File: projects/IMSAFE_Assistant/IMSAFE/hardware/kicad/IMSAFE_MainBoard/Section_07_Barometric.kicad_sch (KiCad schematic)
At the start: 3 parts, among them U9 BMP390

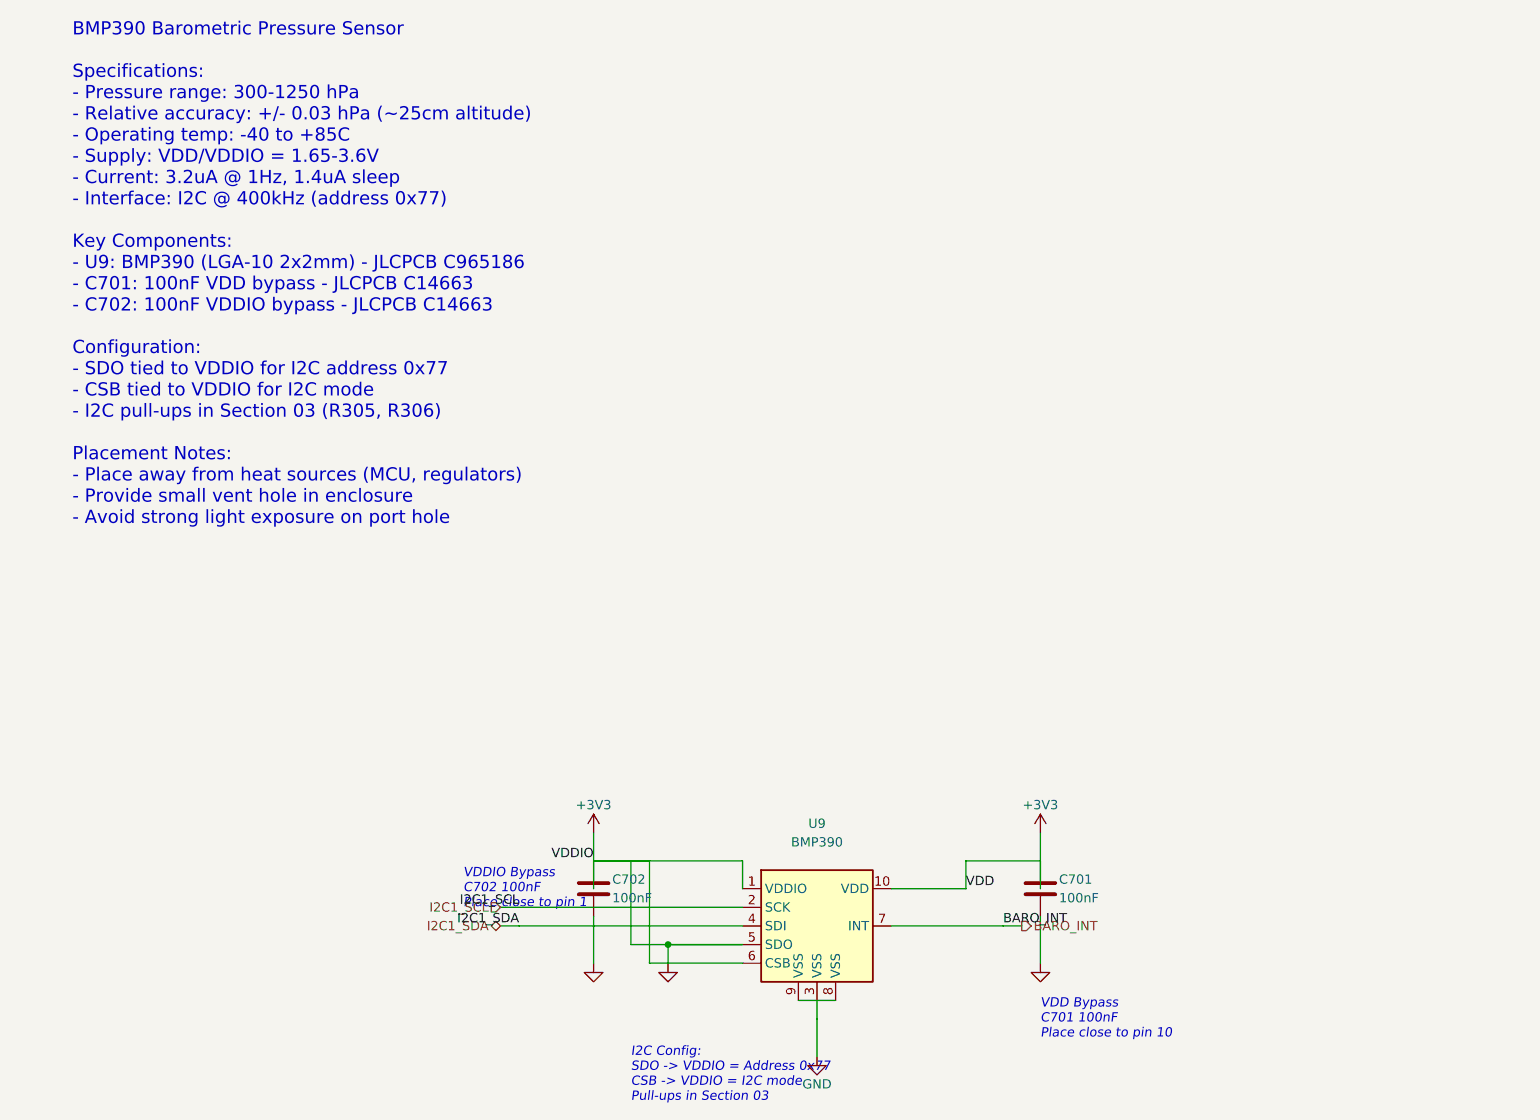
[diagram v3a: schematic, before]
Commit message: Update KiCad schematics and add analysis files
- Update all MainBoard schematic sections with component placement
- Add ERC reports and analysis scripts for schematic validation
- Update Radar Interface and SwitchLED Board projects
- Sync KiCad project files with latest session changes

Co-Authored-By: Claude Opus 4.5 <noreply@anthropic.com>
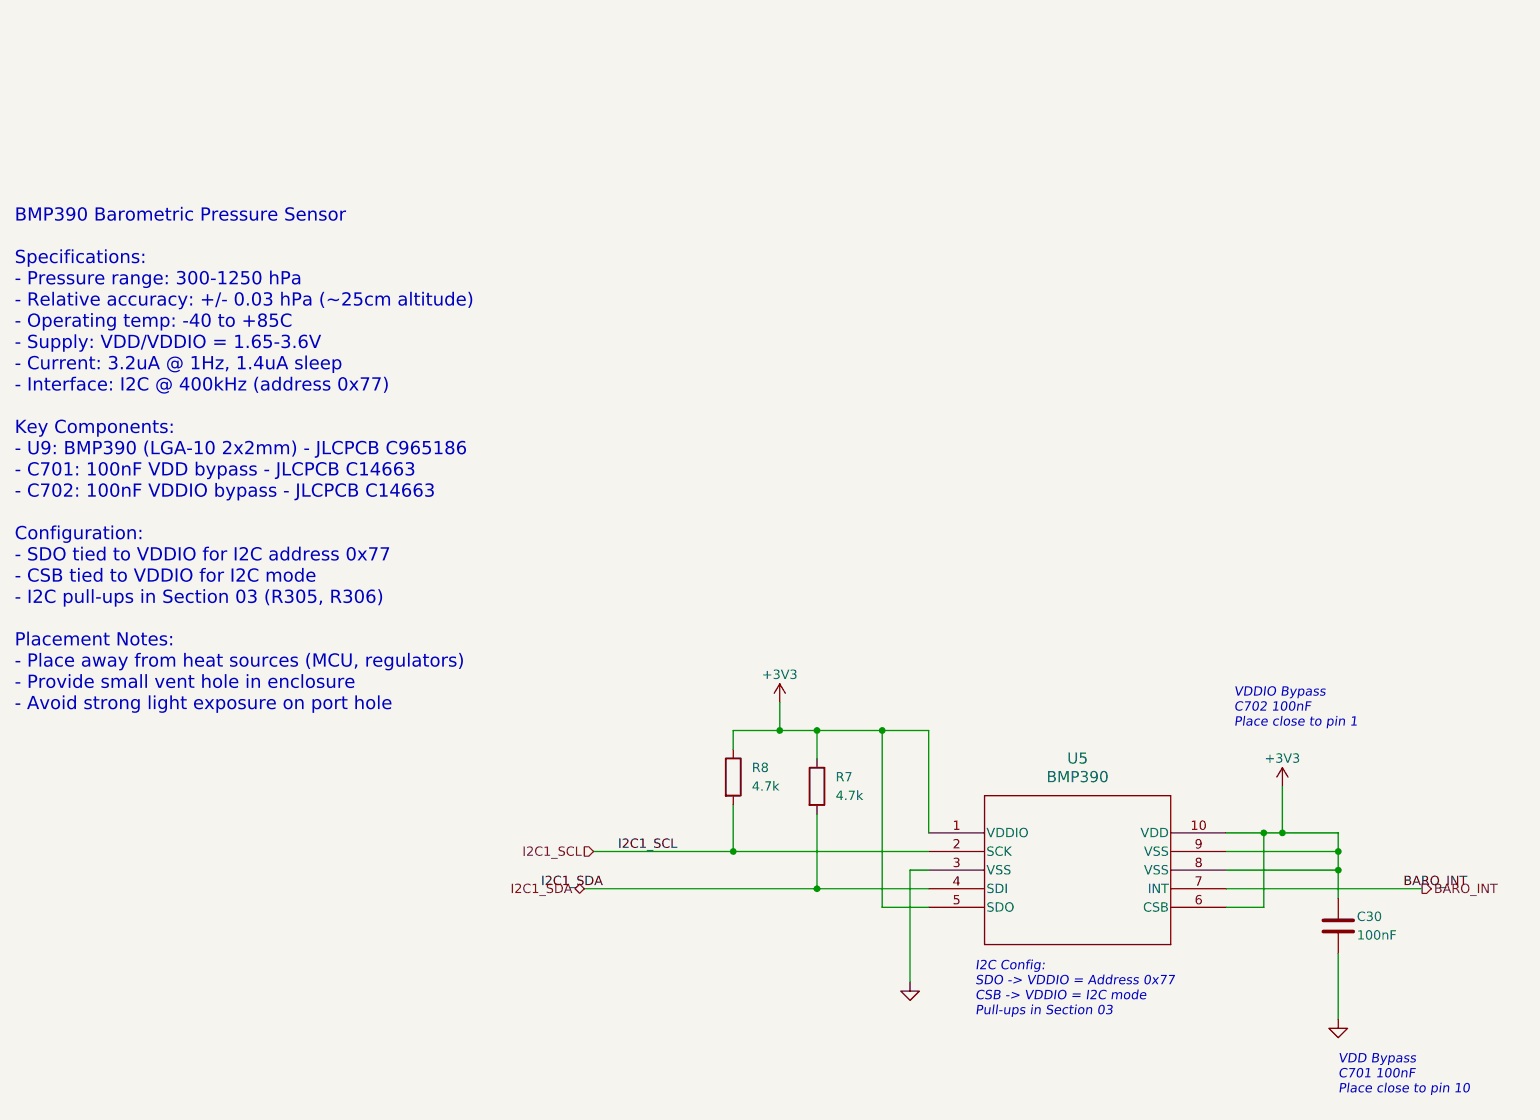
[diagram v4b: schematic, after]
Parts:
- removed C701, C702: 100nF, Capacitor_SMD:C_0603_1608Metric, symbol Device:C
- removed U9: BMP390, Package_LGA:Bosch_LGA-10_2x2.5mm_P0.5mm, symbol Sensor:BMP390
- added C30: 100nF, Capacitor_SMD:C_0603_1608Metric, symbol Device:C
- added R7, R8: 4.7k, Resistor_SMD:R_0603_1608Metric, symbol Device:R
- added U5: BMP390, 10LGA_2X2X0p75_BOS, symbol 1_New_library:BMP390
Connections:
- net +3V3: now also C30.1, R7.1, R8.1, U5.1 (VDDIO), U5.10 (VDD), U5.5 (SDO), U5.6 (CSB), U5.8 (VSS), U5.9 (VSS)
- net BARO_INT: now also U5.7 (INT)
- net I2C1_SCL: now also R8.2, U5.2 (SCK)
- net I2C1_SDA: now also R7.2, U5.4 (SDI)
- new net GND: C30.2, U5.3 (VSS)
